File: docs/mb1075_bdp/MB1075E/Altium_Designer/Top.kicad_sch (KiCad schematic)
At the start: 6 parts, among them P1 Header 32X2, P2 Header 32X2

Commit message: save before i break everything out instead idk why i didnt do that
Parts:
- removed HW8: STICKER_PRODUCT, symbol MB1075:U_Top_0_STICKER_PRODUCT_MB1075.SCHLIB
- removed HW9: STICKER_BOARD, symbol MB1075:U_Top_0_STICKER_BOARD_MB1075.SCHLIB
- removed P1, P2: Header 32X2, HDR2X32, symbol MCD_TOOLS:U_Top_0_Header 32X2_MCD_TOOLS.SchLib
- removed SB26, SB27: Circuit Breaker, JP2_SMD, symbol MCD_TOOLS:U_Top_0_Circuit Breaker_MCD_TOOLS.SCHLIB
- added HW8: STICKER_PRODUCT, symbol MB1075:root_0_STICKER_PRODUCT_MB1075.SCHLIB
- added HW9: STICKER_BOARD, symbol MB1075:root_0_STICKER_BOARD_MB1075.SCHLIB
- added P1, P2: Header 32X2, HDR2X32, symbol MCD_TOOLS:root_0_Header 32X2_MCD_TOOLS.SchLib
- added SB26, SB27: Circuit Breaker, JP2_SMD, symbol MCD_TOOLS:root_0_Circuit Breaker_MCD_TOOLS.SCHLIB
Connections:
- net 3V: now also P2.1, P2.2
- net 5V: now also P1.1, P1.2
- net BOOT0: now also P1.21
- net GND: now also P1.63, P1.64, P2.11, P2.29, P2.63, P2.64
- net NRST: now also P2.12
- net PA0: now also P2.18
- net PA1: now also P2.17
- net PA10: now also P1.51
- net PA11: now also P1.50
- net PA12: now also P1.49
- net PA13: now also P1.48
- net PA14: now also P1.47
- net PA15: now also P1.46
- net PA2: now also P2.20
- net PA3: now also P2.19
- net PA4: now also P2.22
- net PA5: now also P2.21
- net PA6: now also P2.24
- net PA7: now also P2.23
- net PA8: now also P1.53
- net PA9: now also P1.52
- net PB0: now also P2.28
- net PB1: now also P2.27
- net PB10: now also P2.48
- net PB11: now also P2.47
- net PB12: now also P2.50
- net PB13: now also P2.49
- net PB14: now also SB27.2
- net PB15: now also SB26.1
- net PB2: now also P2.30
- net PB3: now also P1.28
- net PB4: now also P1.25
- net PB5: now also P1.26
- net PB6: now also P1.23
- net PB7: now also P1.24
- net PB8: now also P1.19
- net PB9: now also P1.20
- net PC0: now also P2.14
- net PC1: now also P2.13
- net PC10: now also P1.45
- net PC11: now also P1.44
- net PC12: now also P1.43
- net PC13: now also P1.12
- net PC14: now also P1.9
- net PC15: now also P1.10
- net PC2: now also P2.16
- net PC3: now also P2.15
- net PC4: now also P2.26
- net PC5: now also P2.25
- net PC6: now also P1.57
- net PC7: now also P1.56
- net PC8: now also P1.55
- net PC9: now also P1.54
- net PD0: now also P1.42
- net PD1: now also P1.41
- net PD10: now also P2.56
- net PD11: now also P2.55
- net PD12: now also P2.58
- net PD13: now also P2.57
- net PD14: now also P2.60
- net PD15: now also P2.59
- net PD2: now also P1.40
- net PD3: now also P1.39
- net PD4: now also P1.38
- net PD5: now also P1.37
- net PD6: now also P1.36
- net PD7: now also P1.35
- net PD8: now also P2.54
- net PD9: now also P2.53
- net PE0: now also P1.17
- net PE1: now also P1.18
- net PE10: now also P2.42
- net PE11: now also P2.41
- net PE12: now also P2.44
- net PE13: now also P2.43
- net PE14: now also P2.46
- net PE15: now also P2.45
- net PE2: now also P1.15
- net PE3: now also P1.16
- net PE4: now also P1.13
- net PE5: now also P1.14
- net PE6: now also P1.11
- net PE7: now also P2.37
- net PE8: now also P2.40
- net PE9: now also P2.39
- net PF0: now also P1.7
- net PF1: now also P1.8
- net PF10: now also P2.7
- net PF11: now also P2.32
- net PF12: now also P2.31
- net PF13: now also P2.34
- net PF14: now also P2.33
- net PF15: now also P2.36
- net PF2: now also P1.5
- net PF3: now also P1.6
- net PF4: now also P1.3
- net PF5: now also P1.4
- net PF6: now also P2.3
- net PF7: now also P2.6
- net PF8: now also P2.5
- net PF9: now also P2.8
- net PG0: now also P2.35
- net PG1: now also P2.38
- net PG10: now also P1.34
- net PG11: now also P1.31
- net PG12: now also P1.32
- net PG13: now also P1.29
- net PG14: now also P1.30
- net PG15: now also P1.27
- net PG2: now also P2.62
- net PG3: now also P2.61
- net PG4: now also P1.62
- net PG5: now also P1.61
- net PG6: now also P1.60
- net PG7: now also P1.59
- net PG8: now also P1.58
- net PG9: now also P1.33
- net PH0: now also P2.10
- net PH1: now also P2.9
- net VDD: now also P1.22
- new net: P2.51, SB26.2
- new net: P2.52, SB27.1
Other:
- sheet U_IO_Peripherals: file IO_Peripherals.SchDoc -> IO_Peripherals.kicad_sch
- sheet U_LCD-24: file LCD-24.SchDoc -> LCD-24.kicad_sch

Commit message: KILL ME!!!!!!!!!!!
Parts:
- removed HW8: STICKER_PRODUCT, symbol MB1075:root_0_STICKER_PRODUCT_MB1075.SCHLIB
- removed HW9: STICKER_BOARD, symbol MB1075:root_0_STICKER_BOARD_MB1075.SCHLIB
- removed P1, P2: Header 32X2, HDR2X32, symbol MCD_TOOLS:root_0_Header 32X2_MCD_TOOLS.SchLib
- removed SB26, SB27: Circuit Breaker, JP2_SMD, symbol MCD_TOOLS:root_0_Circuit Breaker_MCD_TOOLS.SCHLIB
- added HW8: STICKER_PRODUCT, symbol MB1075:U_Top_0_STICKER_PRODUCT_MB1075.SCHLIB
- added HW9: STICKER_BOARD, symbol MB1075:U_Top_0_STICKER_BOARD_MB1075.SCHLIB
- added P1, P2: Header 32X2, HDR2X32, symbol MCD_TOOLS:U_Top_0_Header 32X2_MCD_TOOLS.SchLib
- added SB26, SB27: Circuit Breaker, JP2_SMD, symbol MCD_TOOLS:U_Top_0_Circuit Breaker_MCD_TOOLS.SCHLIB
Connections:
- net 3V: now also P2.1, P2.2
- net 5V: now also P1.1, P1.2
- net BOOT0: now also P1.21
- net GND: now also P1.63, P1.64, P2.11, P2.29, P2.63, P2.64
- net NRST: now also P2.12
- net PA0: now also P2.18
- net PA1: now also P2.17
- net PA10: now also P1.51
- net PA11: now also P1.50
- net PA12: now also P1.49
- net PA13: now also P1.48
- net PA14: now also P1.47
- net PA15: now also P1.46
- net PA2: now also P2.20
- net PA3: now also P2.19
- net PA4: now also P2.22
- net PA5: now also P2.21
- net PA6: now also P2.24
- net PA7: now also P2.23
- net PA8: now also P1.53
- net PA9: now also P1.52
- net PB0: now also P2.28
- net PB1: now also P2.27
- net PB10: now also P2.48
- net PB11: now also P2.47
- net PB12: now also P2.50
- net PB13: now also P2.49
- net PB14: now also SB27.2
- net PB15: now also SB26.1
- net PB2: now also P2.30
- net PB3: now also P1.28
- net PB4: now also P1.25
- net PB5: now also P1.26
- net PB6: now also P1.23
- net PB7: now also P1.24
- net PB8: now also P1.19
- net PB9: now also P1.20
- net PC0: now also P2.14
- net PC1: now also P2.13
- net PC10: now also P1.45
- net PC11: now also P1.44
- net PC12: now also P1.43
- net PC13: now also P1.12
- net PC14: now also P1.9
- net PC15: now also P1.10
- net PC2: now also P2.16
- net PC3: now also P2.15
- net PC4: now also P2.26
- net PC5: now also P2.25
- net PC6: now also P1.57
- net PC7: now also P1.56
- net PC8: now also P1.55
- net PC9: now also P1.54
- net PD0: now also P1.42
- net PD1: now also P1.41
- net PD10: now also P2.56
- net PD11: now also P2.55
- net PD12: now also P2.58
- net PD13: now also P2.57
- net PD14: now also P2.60
- net PD15: now also P2.59
- net PD2: now also P1.40
- net PD3: now also P1.39
- net PD4: now also P1.38
- net PD5: now also P1.37
- net PD6: now also P1.36
- net PD7: now also P1.35
- net PD8: now also P2.54
- net PD9: now also P2.53
- net PE0: now also P1.17
- net PE1: now also P1.18
- net PE10: now also P2.42
- net PE11: now also P2.41
- net PE12: now also P2.44
- net PE13: now also P2.43
- net PE14: now also P2.46
- net PE15: now also P2.45
- net PE2: now also P1.15
- net PE3: now also P1.16
- net PE4: now also P1.13
- net PE5: now also P1.14
- net PE6: now also P1.11
- net PE7: now also P2.37
- net PE8: now also P2.40
- net PE9: now also P2.39
- net PF0: now also P1.7
- net PF1: now also P1.8
- net PF10: now also P2.7
- net PF11: now also P2.32
- net PF12: now also P2.31
- net PF13: now also P2.34
- net PF14: now also P2.33
- net PF15: now also P2.36
- net PF2: now also P1.5
- net PF3: now also P1.6
- net PF4: now also P1.3
- net PF5: now also P1.4
- net PF6: now also P2.3
- net PF7: now also P2.6
- net PF8: now also P2.5
- net PF9: now also P2.8
- net PG0: now also P2.35
- net PG1: now also P2.38
- net PG10: now also P1.34
- net PG11: now also P1.31
- net PG12: now also P1.32
- net PG13: now also P1.29
- net PG14: now also P1.30
- net PG15: now also P1.27
- net PG2: now also P2.62
- net PG3: now also P2.61
- net PG4: now also P1.62
- net PG5: now also P1.61
- net PG6: now also P1.60
- net PG7: now also P1.59
- net PG8: now also P1.58
- net PG9: now also P1.33
- net PH0: now also P2.10
- net PH1: now also P2.9
- net VDD: now also P1.22
- new net: P2.52, SB27.1
- new net: P2.51, SB26.2
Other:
- sheet U_IO_Peripherals: file IO_Peripherals.kicad_sch -> IO_Peripherals.SchDoc
- sheet U_LCD-24: file LCD-24.kicad_sch -> LCD-24.SchDoc

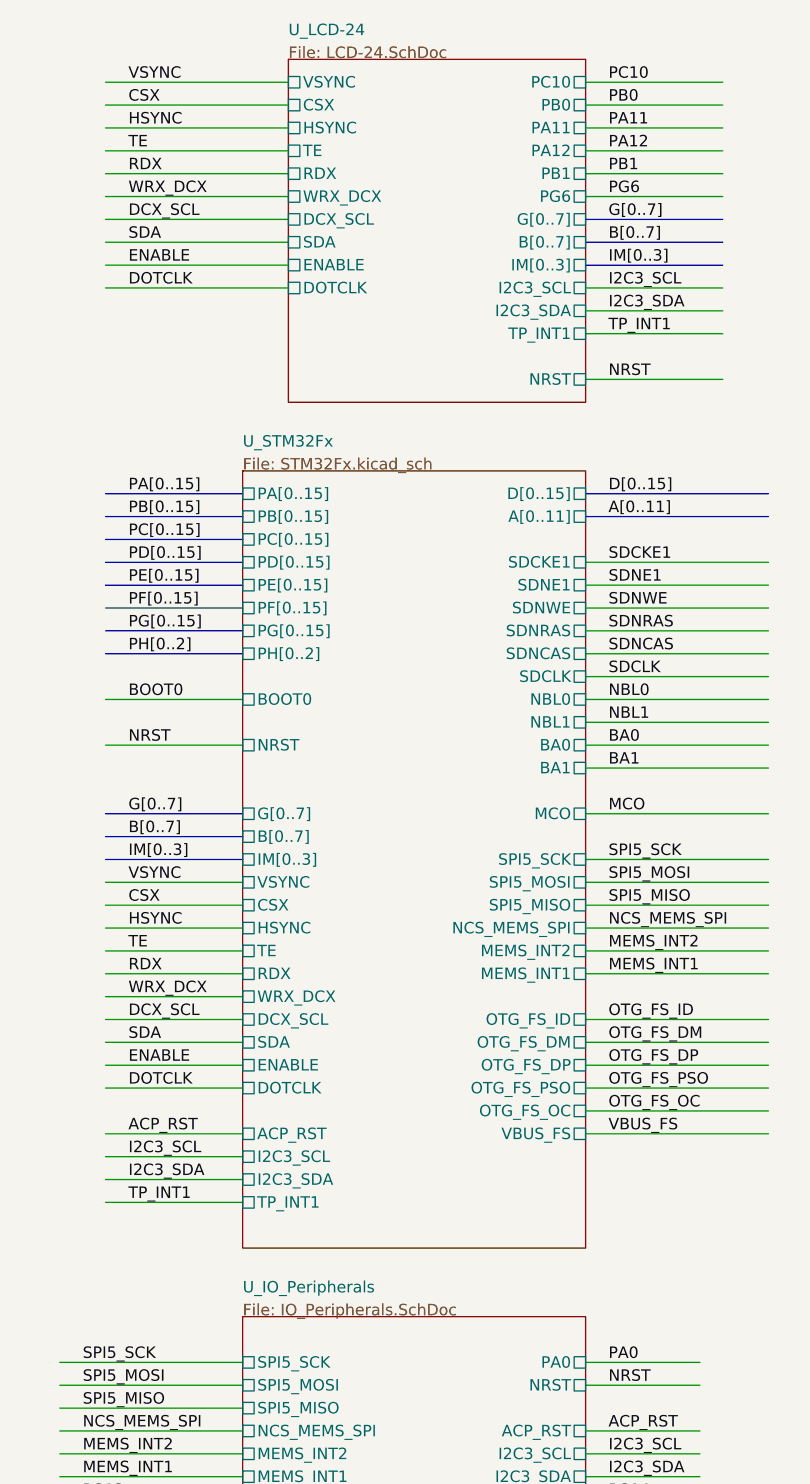
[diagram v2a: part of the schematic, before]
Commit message: esd protection for usb data lines
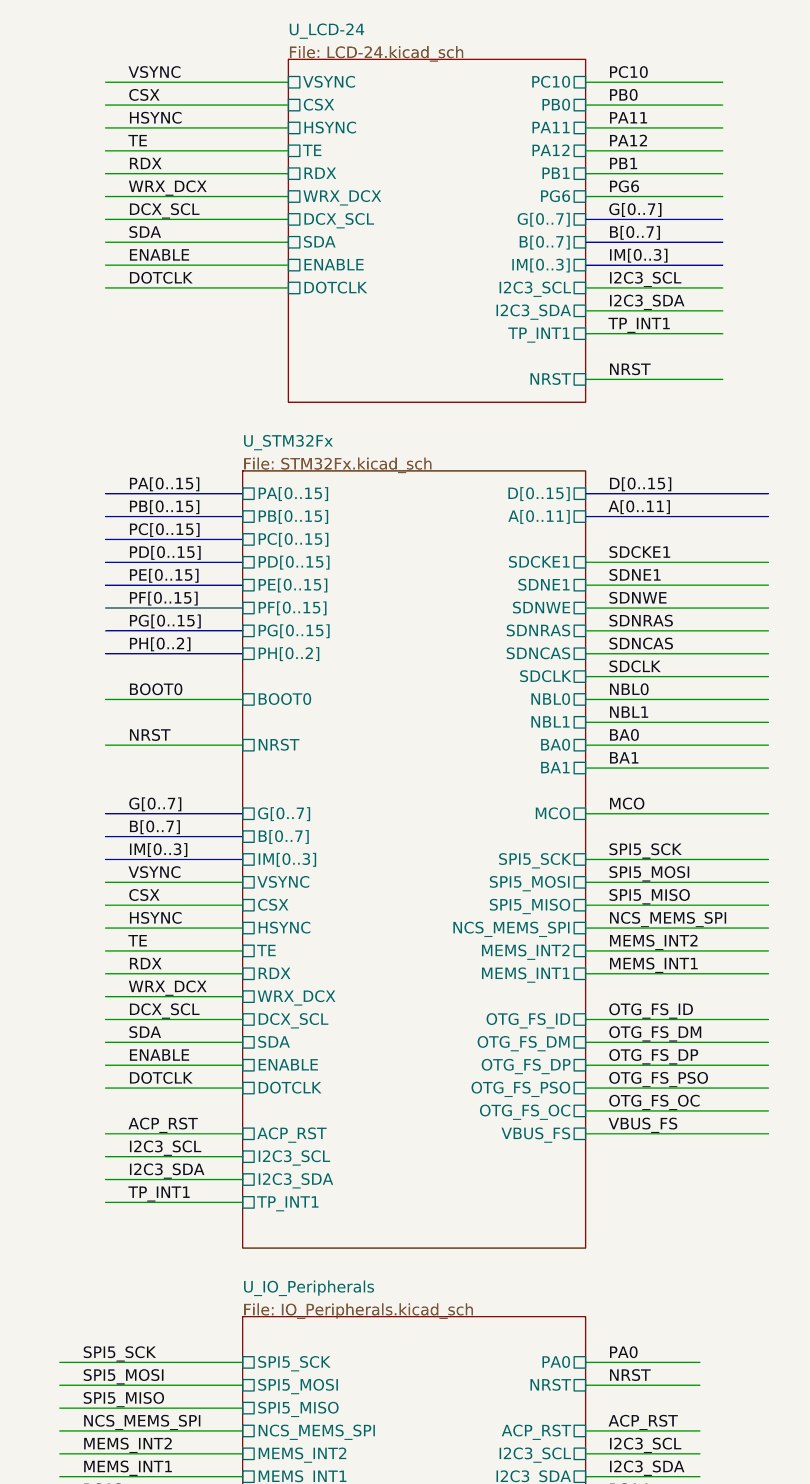
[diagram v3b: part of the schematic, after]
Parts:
- removed HW8: STICKER_PRODUCT, symbol MB1075:U_Top_0_STICKER_PRODUCT_MB1075.SCHLIB
- removed HW9: STICKER_BOARD, symbol MB1075:U_Top_0_STICKER_BOARD_MB1075.SCHLIB
- removed P1, P2: Header 32X2, HDR2X32, symbol MCD_TOOLS:U_Top_0_Header 32X2_MCD_TOOLS.SchLib
- removed SB26, SB27: Circuit Breaker, JP2_SMD, symbol MCD_TOOLS:U_Top_0_Circuit Breaker_MCD_TOOLS.SCHLIB
- added HW8: STICKER_PRODUCT, symbol MB1075:root_0_STICKER_PRODUCT_MB1075.SCHLIB
- added HW9: STICKER_BOARD, symbol MB1075:root_0_STICKER_BOARD_MB1075.SCHLIB
- added P1, P2: Header 32X2, HDR2X32, symbol MCD_TOOLS:root_0_Header 32X2_MCD_TOOLS.SchLib
- added SB26, SB27: Circuit Breaker, JP2_SMD, symbol MCD_TOOLS:root_0_Circuit Breaker_MCD_TOOLS.SCHLIB
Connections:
- net 3V: now also P2.1, P2.2
- net 5V: now also P1.1, P1.2
- net BOOT0: now also P1.21
- net GND: now also P1.63, P1.64, P2.11, P2.29, P2.63, P2.64
- net NRST: now also P2.12
- net PA0: now also P2.18
- net PA1: now also P2.17
- net PA10: now also P1.51
- net PA11: now also P1.50
- net PA12: now also P1.49
- net PA13: now also P1.48
- net PA14: now also P1.47
- net PA15: now also P1.46
- net PA2: now also P2.20
- net PA3: now also P2.19
- net PA4: now also P2.22
- net PA5: now also P2.21
- net PA6: now also P2.24
- net PA7: now also P2.23
- net PA8: now also P1.53
- net PA9: now also P1.52
- net PB0: now also P2.28
- net PB1: now also P2.27
- net PB10: now also P2.48
- net PB11: now also P2.47
- net PB12: now also P2.50
- net PB13: now also P2.49
- net PB14: now also SB27.2
- net PB15: now also SB26.1
- net PB2: now also P2.30
- net PB3: now also P1.28
- net PB4: now also P1.25
- net PB5: now also P1.26
- net PB6: now also P1.23
- net PB7: now also P1.24
- net PB8: now also P1.19
- net PB9: now also P1.20
- net PC0: now also P2.14
- net PC1: now also P2.13
- net PC10: now also P1.45
- net PC11: now also P1.44
- net PC12: now also P1.43
- net PC13: now also P1.12
- net PC14: now also P1.9
- net PC15: now also P1.10
- net PC2: now also P2.16
- net PC3: now also P2.15
- net PC4: now also P2.26
- net PC5: now also P2.25
- net PC6: now also P1.57
- net PC7: now also P1.56
- net PC8: now also P1.55
- net PC9: now also P1.54
- net PD0: now also P1.42
- net PD1: now also P1.41
- net PD10: now also P2.56
- net PD11: now also P2.55
- net PD12: now also P2.58
- net PD13: now also P2.57
- net PD14: now also P2.60
- net PD15: now also P2.59
- net PD2: now also P1.40
- net PD3: now also P1.39
- net PD4: now also P1.38
- net PD5: now also P1.37
- net PD6: now also P1.36
- net PD7: now also P1.35
- net PD8: now also P2.54
- net PD9: now also P2.53
- net PE0: now also P1.17
- net PE1: now also P1.18
- net PE10: now also P2.42
- net PE11: now also P2.41
- net PE12: now also P2.44
- net PE13: now also P2.43
- net PE14: now also P2.46
- net PE15: now also P2.45
- net PE2: now also P1.15
- net PE3: now also P1.16
- net PE4: now also P1.13
- net PE5: now also P1.14
- net PE6: now also P1.11
- net PE7: now also P2.37
- net PE8: now also P2.40
- net PE9: now also P2.39
- net PF0: now also P1.7
- net PF1: now also P1.8
- net PF10: now also P2.7
- net PF11: now also P2.32
- net PF12: now also P2.31
- net PF13: now also P2.34
- net PF14: now also P2.33
- net PF15: now also P2.36
- net PF2: now also P1.5
- net PF3: now also P1.6
- net PF4: now also P1.3
- net PF5: now also P1.4
- net PF6: now also P2.3
- net PF7: now also P2.6
- net PF8: now also P2.5
- net PF9: now also P2.8
- net PG0: now also P2.35
- net PG1: now also P2.38
- net PG10: now also P1.34
- net PG11: now also P1.31
- net PG12: now also P1.32
- net PG13: now also P1.29
- net PG14: now also P1.30
- net PG15: now also P1.27
- net PG2: now also P2.62
- net PG3: now also P2.61
- net PG4: now also P1.62
- net PG5: now also P1.61
- net PG6: now also P1.60
- net PG7: now also P1.59
- net PG8: now also P1.58
- net PG9: now also P1.33
- net PH0: now also P2.10
- net PH1: now also P2.9
- net VDD: now also P1.22
- new net: P2.51, SB26.2
- new net: P2.52, SB27.1
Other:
- sheet U_IO_Peripherals: file IO_Peripherals.SchDoc -> IO_Peripherals.kicad_sch
- sheet U_LCD-24: file LCD-24.SchDoc -> LCD-24.kicad_sch
